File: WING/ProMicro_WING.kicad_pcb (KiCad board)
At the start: 2 copper layers, 23.4 x 51.4 mm, 8 parts, among them U1 Adafruit_HUZZAH32_ESP32_Feath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, U2 Adafruit_Feather_HUZZAH_ESP82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

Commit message: clean
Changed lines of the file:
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@@
     (fp_arc (start 19.05 42.05) (end 19.05 44.84) (angle -90) (layer F.CrtYd) (width 0.05))
     (fp_arc (start 1.27 42.05) (end -1.52 42.05) (angle -90) (layer F.CrtYd) (width 0.05))
-    (pad 1 thru_hole rect (at 0 0) (size 1.6 1.6) (drill 0.8) (layers *.Cu *.Mask))
-    (pad 2 thru_hole circle (at 0 2.54) (size 1.6 1.6) (drill 0.8) (layers *.Cu *.Mask)
+    (pad 1 thru_hole rect (at 0 0) (size 2 2) (drill 1) (layers *.Cu *.Mask))
+    (pad 2 thru_hole circle (at 0 2.54) (size 2 2) (drill 1) (layers *.Cu *.Mask)
       (net 23 EN))
-    (pad 3 thru_hole circle (at 0 5.08) (size 1.6 1.6) (drill 0.8) (layers *.Cu *.Mask)
+    (pad 3 thru_hole circle (at 0 5.08) (size 2 2) (drill 1) (layers *.Cu *.Mask)
       (net 22 +5V))
-    (pad 4 thru_hole circle (at 0 7.62) (size 1.6 1.6) (drill 0.8) (layers *.Cu *.Mask)
+    (pad 4 thru_hole circle (at 0 7.62) (size 2 2) (drill 1) (layers *.Cu *.Mask)
       (net 6 A3))
-    (pad 5 thru_hole circle (at 0 10.16) (size 1.6 1.6) (drill 0.8) (layers *.Cu *.Mask)
+    (pad 5 thru_hole circle (at 0 10.16) (size 2 2) (drill 1) (layers *.Cu *.Mask)
       (net 12 A0))
-    (pad 6 thru_hole circle (at 0 12.7) (size 1.6 1.6) (drill 0.8) (layers *.Cu *.Mask)
+    (pad 6 thru_hole circle (at 0 12.7) (size 2 2) (drill 1) (layers *.Cu *.Mask)
       (net 18 D16))
-    (pad 7 thru_hole circle (at 0 15.24) (size 1.6 1.6) (drill 0.8) (layers *.Cu *.Mask)
+    (pad 7 thru_hole circle (at 0 15.24) (size 2 2) (drill 1) (layers *.Cu *.Mask)
       (net 19 D10))
-    (pad 8 thru_hole circle (at 0 17.78) (size 1.6 1.6) (drill 0.8) (layers *.Cu *.Mask)
+    (pad 8 thru_hole circle (at 0 17.78) (size 2 2) (drill 1) (layers *.Cu *.Mask)
       (net 10 A1))
-    (pad 9 thru_hole circle (at 0 20.32) (size 1.6 1.6) (drill 0.8) (layers *.Cu *.Mask)
+    (pad 9 thru_hole circle (at 0 20.32) (size 2 2) (drill 1) (layers *.Cu *.Mask)
       (net 7 D7))
-    (pad 10 thru_hole circle (at 0 22.86) (size 1.6 1.6) (drill 0.8) (layers *.Cu *.Mask)
+    (pad 10 thru_hole circle (at 0 22.86) (size 2 2) (drill 1) (layers *.Cu *.Mask)
       (net 8 A2))
-    (pad 11 thru_hole circle (at 0 25.4) (size 1.6 1.6) (drill 0.8) (layers *.Cu *.Mask)
+    (pad 11 thru_hole circle (at 0 25.4) (size 2 2) (drill 1) (layers *.Cu *.Mask)
       (net 15 D3))
-    (pad 12 thru_hole circle (at 0 27.94) (size 1.6 1.6) (drill 0.8) (layers *.Cu *.Mask)
+    (pad 12 thru_hole circle (at 0 27.94) (size 2 2) (drill 1) (layers *.Cu *.Mask)
       (net 17 D2))
-    (pad 13 thru_hole circle (at 20.32 38.1) (size 1.6 1.6) (drill 0.8) (layers *.Cu *.Mask))
-    (pad 14 thru_hole circle (at 20.32 35.56) (size 1.6 1.6) (drill 0.8) (layers *.Cu *.Mask)
+    (pad 13 thru_hole circle (at 20.32 38.1) (size 2 2) (drill 1) (layers *.Cu *.Mask))
+    (pad 14 thru_hole circle (at 20.32 35.56) (size 2 2) (drill 1) (layers *.Cu *.Mask)
       (net 21 D1))
-    (pad 15 thru_hole circle (at 20.32 33.02) (size 1.6 1.6) (drill 0.8) (layers *.Cu *.Mask)
+    (pad 15 thru_hole circle (at 20.32 33.02) (size 2 2) (drill 1) (layers *.Cu *.Mask)
       (net 20 D0))
-    (pad 16 thru_hole circle (at 20.32 30.48) (size 1.6 1.6) (drill 0.8) (layers *.Cu *.Mask)
+    (pad 16 thru_hole circle (at 20.32 30.48) (size 2 2) (drill 1) (layers *.Cu *.Mask)
       (net 16 D14))
-    (pad 17 thru_hole circle (at 20.32 27.94) (size 1.6 1.6) (drill 0.8) (layers *.Cu *.Mask)
+    (pad 17 thru_hole circle (at 20.32 27.94) (size 2 2) (drill 1) (layers *.Cu *.Mask)
       (net 18 D16))
-    (pad 18 thru_hole circle (at 20.32 25.4) (size 1.6 1.6) (drill 0.8) (layers *.Cu *.Mask)
+    (pad 18 thru_hole circle (at 20.32 25.4) (size 2 2) (drill 1) (layers *.Cu *.Mask)
       (net 14 D15))
-    (pad 19 thru_hole circle (at 20.32 22.86) (size 1.6 1.6) (drill 0.8) (layers *.Cu *.Mask))
-    (pad 20 thru_hole circle (at 20.32 20.32) (size 1.6 1.6) (drill 0.8) (layers *.Cu *.Mask))
-    (pad 21 thru_hole circle (at 20.32 17.78) (size 1.6 1.6) (drill 0.8) (layers *.Cu *.Mask))
-    (pad 22 thru_hole circle (at 20.32 15.24) (size 1.6 1.6) (drill 0.8) (layers *.Cu *.Mask))
-    (pad 23 thru_hole circle (at 20.32 12.7) (size 1.6 1.6) (drill 0.8) (layers *.Cu *.Mask))
-    (pad 25 thru_hole circle (at 20.32 7.62) (size 1.6 1.6) (drill 0.8) (layers *.Cu *.Mask)
+    (pad 19 thru_hole circle (at 20.32 22.86) (size 2 2) (drill 1) (layers *.Cu *.Mask))
+    (pad 20 thru_hole circle (at 20.32 20.32) (size 2 2) (drill 1) (layers *.Cu *.Mask))
+    (pad 21 thru_hole circle (at 20.32 17.78) (size 2 2) (drill 1) (layers *.Cu *.Mask))
+    (pad 22 thru_hole circle (at 20.32 15.24) (size 2 2) (drill 1) (layers *.Cu *.Mask))
+    (pad 23 thru_hole circle (at 20.32 12.7) (size 2 2) (drill 1) (layers *.Cu *.Mask))
+    (pad 25 thru_hole circle (at 20.32 7.62) (size 2 2) (drill 1) (layers *.Cu *.Mask)
       (net 1 GND))
-    (pad 26 thru_hole circle (at 20.32 5.08) (size 1.6 1.6) (drill 0.8) (layers *.Cu *.Mask))
-    (pad 27 thru_hole circle (at 20.32 2.54) (size 1.6 1.6) (drill 0.8) (layers *.Cu *.Mask)
+    (pad 26 thru_hole circle (at 20.32 5.08) (size 2 2) (drill 1) (layers *.Cu *.Mask))
+    (pad 27 thru_hole circle (at 20.32 2.54) (size 2 2) (drill 1) (layers *.Cu *.Mask)
       (net 2 +3V3))
     (model ${KISYS3DMOD}/Module.3dshapes/Adafruit_Feather.wrl

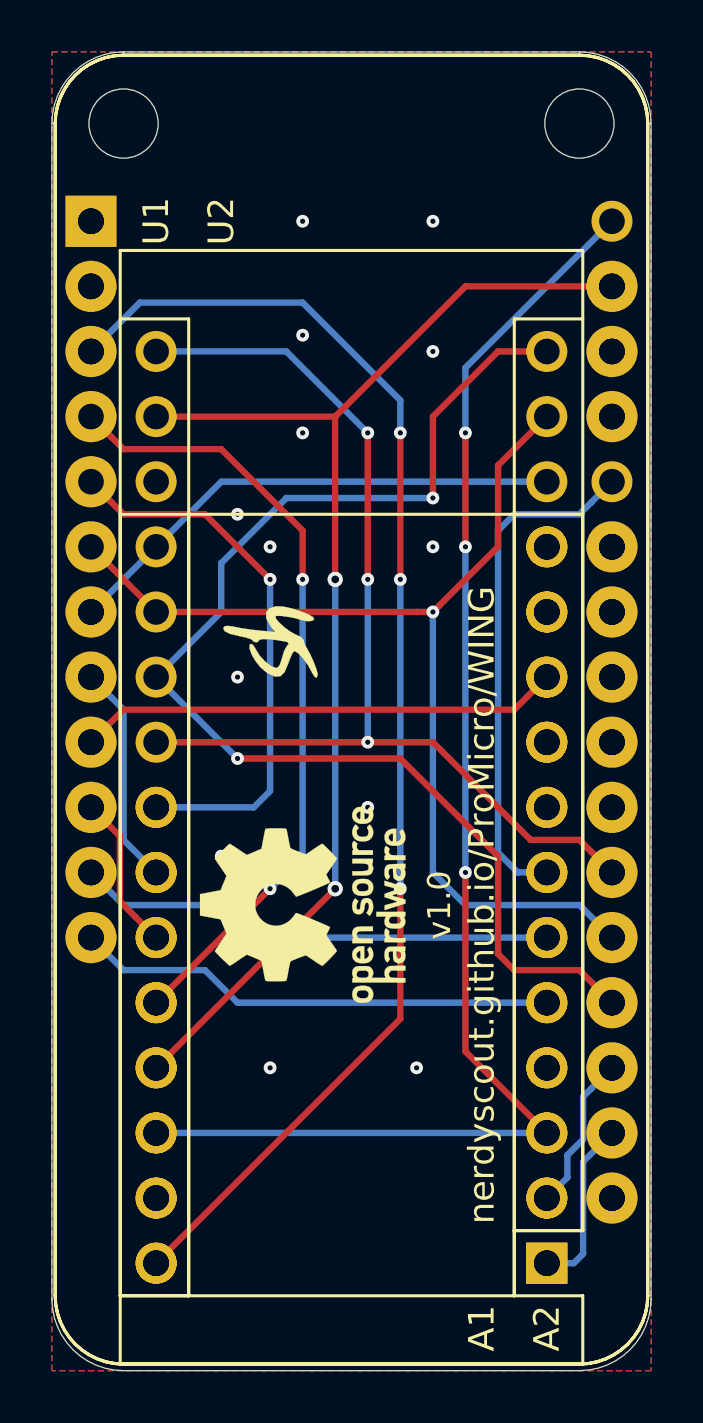
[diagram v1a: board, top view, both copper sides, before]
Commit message: make controller holes wide enough
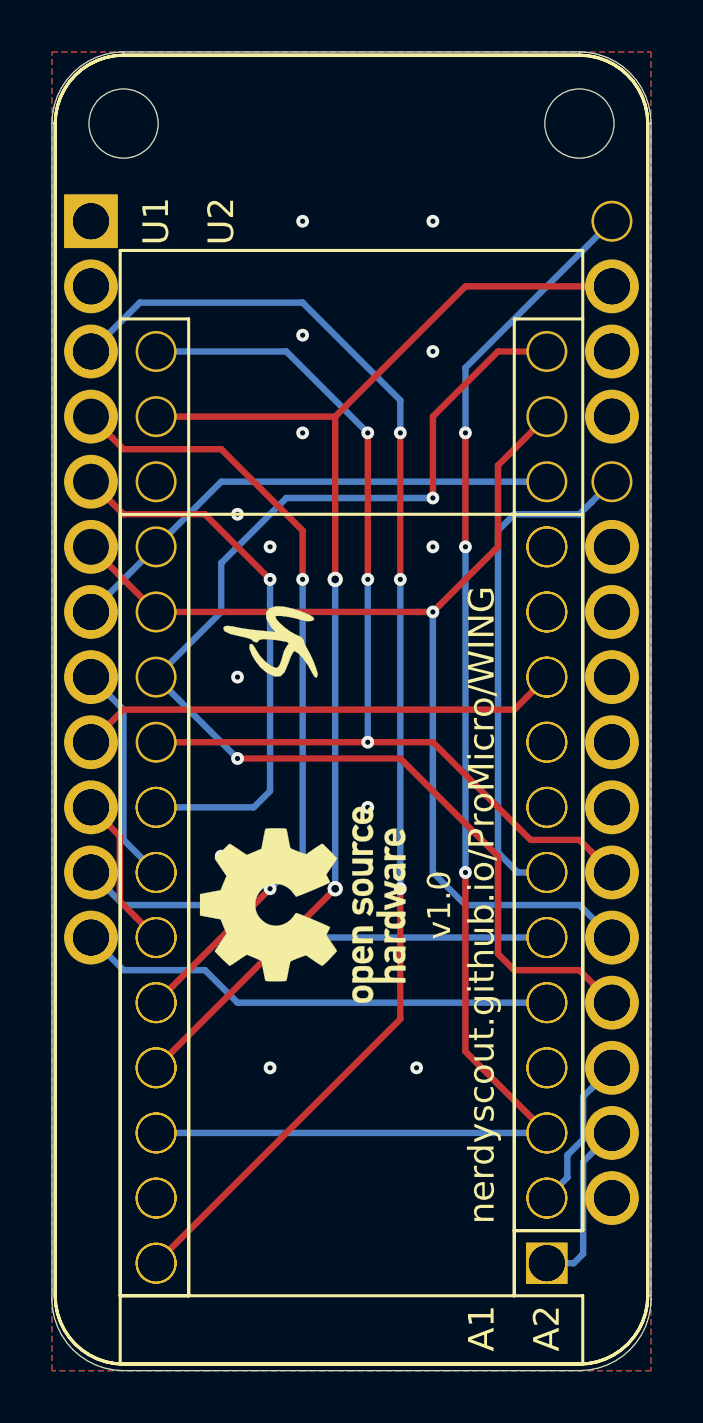
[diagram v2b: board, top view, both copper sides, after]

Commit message: update design
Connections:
- A2 pad 18: (no net) -> Net-(A2-Pad18)
- TP1 pad 1: (no net) -> Net-(TP1-Pad1)
- TP2 pad 1: (no net) -> Net-(TP2-Pad1)
